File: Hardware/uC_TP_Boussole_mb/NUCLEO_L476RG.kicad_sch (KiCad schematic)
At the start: 1 part, among them U2 NUCLEO_L476RG

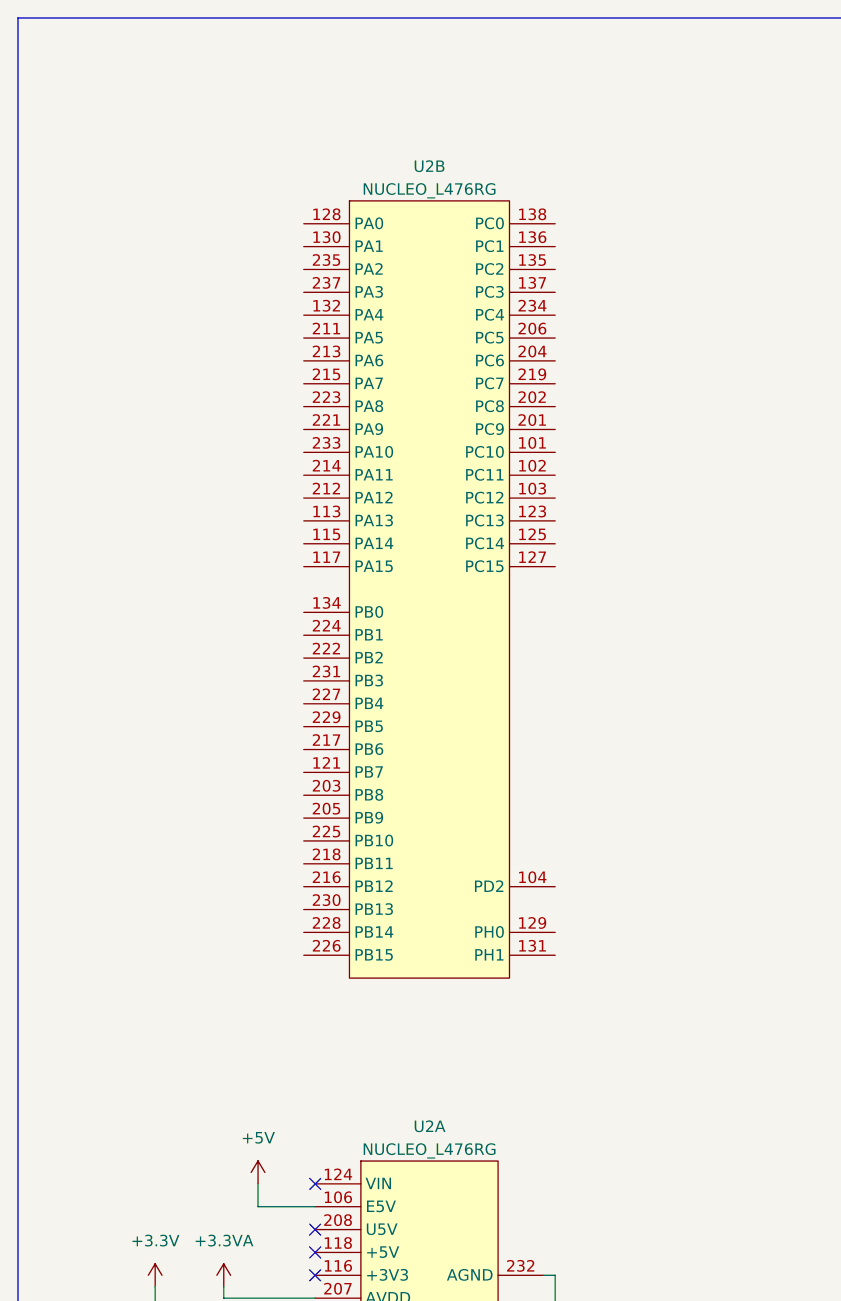
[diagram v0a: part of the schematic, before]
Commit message: starting pin out nucleo
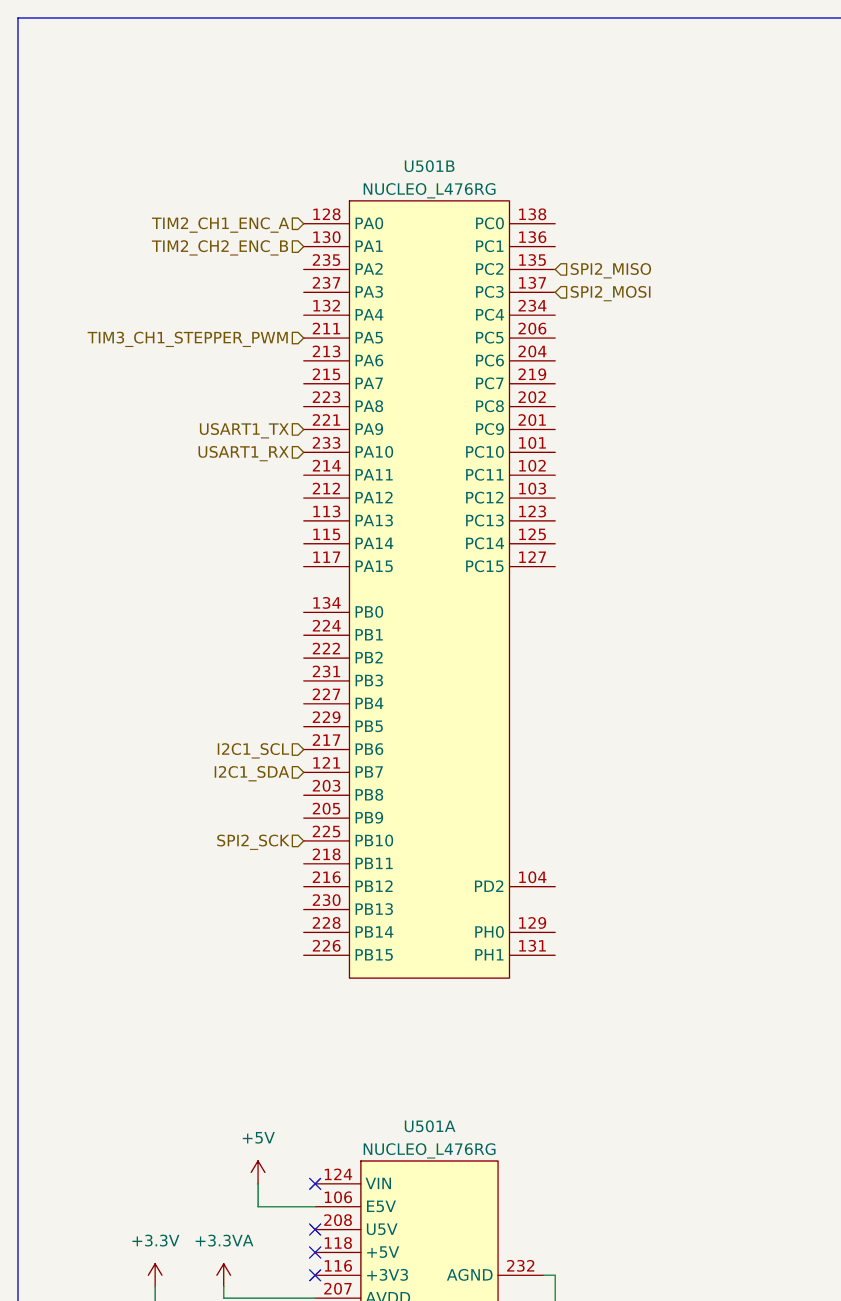
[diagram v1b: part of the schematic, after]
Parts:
- U501: renamed from U2; footprint WITNS:ST_NUCLEO_64 -> libs:ST_NUCLEO_64
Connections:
- net I2C1_SDA: now reaches U501.121 (PB7)
- net TIM2_CH1_ENC_A: now reaches U501.128 (PA0)
- net TIM2_CH2_ENC_B: now reaches U501.130 (PA1)
- net SPI2_MISO: now reaches U501.135 (PC2)
- net SPI2_MOSI: now reaches U501.137 (PC3)
- net TIM3_CH1_STEPPER_PWM: now reaches U501.211 (PA5)
- net I2C1_SCL: now reaches U501.217 (PB6)
- net USART1_TX: now reaches U501.221 (PA9)
- net SPI2_SCK: now reaches U501.225 (PB10)
- net USART1_RX: now reaches U501.233 (PA10)
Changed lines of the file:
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@@
+		)
+	)
+	(hierarchical_label "I2C1_SCL"
+		(shape input)
+		(at 46.99 95.25 180)
+		(fields_autoplaced yes)
+		(effects
+			(font
+				(size 1.27 1.27)
+			)
+			(justify right)
+		)
+	)
+	(hierarchical_label "TIM2_CH1_ENC_A"
+		(shape input)
+		(at 46.99 36.83 180)
+		(fields_autoplaced yes)
+		(effects
+			(font
+				(size 1.27 1.27)
+			)
+			(justify right)
+		)
+	)
+	(hierarchical_label "SPI2_MISO"
+		(shape input)
+		(at 74.93 41.91 0)
+		(fields_autoplaced yes)
+		(effects
+			(font
+				(size 1.27 1.27)
+			)
+			(justify left)
+		)
+	)
+	(hierarchical_label "SPI2_SCK"
+		(shape input)
+		(at 46.99 105.41 180)
+		(fields_autoplaced yes)
+		(effects
+			(font
+				(size 1.27 1.27)
+			)
+			(justify right)
+		)
+	)
+	(hierarchical_label "USART1_TX"
+		(shape input)
+		(at 46.99 59.69 180)
+		(fields_autoplaced yes)
+		(effects
+			(font
+				(size 1.27 1.27)
+			)
+			(justify right)
+		)
+	)
+	(hierarchical_label "TIM2_CH2_ENC_B"
+		(shape input)
+		(at 46.99 39.37 180)
+		(fields_autoplaced yes)
+		(effects
+			(font
+				(size 1.27 1.27)
+			)
+			(justify right)
+		)
+	)
+	(hierarchical_label "I2C1_SDA"
+		(shape input)
+		(at 46.99 97.79 180)
+		(fields_autoplaced yes)
+		(effects
+			(font
+				(size 1.27 1.27)
+			)
+			(justify right)
+		)
+	)
+	(hierarchical_label "SPI2_MOSI"
+		(shape input)
+		(at 74.93 44.45 0)
+		(fields_autoplaced yes)
+		(effects
+			(font
+				(size 1.27 1.27)
+			)
+			(justify left)
+		)
+	)
+	(hierarchical_label "USART1_RX"
+		(shape input)
+		(at 46.99 62.23 180)
+		(fields_autoplaced yes)
+		(effects
+			(font
+				(size 1.27 1.27)
+			)
+			(justify right)
+		)
+	)
+	(hierarchical_label "TIM3_CH1_STEPPER_PWM"
+		(shape input)
+		(at 46.99 49.53 180)
+		(fields_autoplaced yes)
+		(effects
+			(font
+				(size 1.27 1.27)
+			)
+			(justify right)
 		)
 	)
@@
 		(dnp no)
 		(fields_autoplaced yes)
-		(property "Reference" "U2"
+		(property "Reference" "U501"
 			(at 60.96 30.48 0)
 			(effects
@@
 			)
 		)
-		(property "Footprint" "WITNS:ST_NUCLEO_64"
+		(property "Footprint" "libs:ST_NUCLEO_64"
 			(at 60.96 54.61 0)
 			(effects
@@
 			(project "uC_TP_Boussole_mb"
 				(path "/2e9feef3-d2ce-488a-99fa-e1de5099ffc3/05c5487e-de82-4573-ad81-720c1b2881f4"
-					(reference "U2")
+					(reference "U501")
 					(unit 2)
 				)
@@
 		(dnp no)
 		(fields_autoplaced yes)
-		(property "Reference" "#PWR05"
+		(property "Reference" "#PWR0501"
 			(at 30.48 158.75 0)
 			(effects
@@
 			(project "uC_TP_Boussole_mb"
 				(path "/2e9feef3-d2ce-488a-99fa-e1de5099ffc3/05c5487e-de82-4573-ad81-720c1b2881f4"
-					(reference "#PWR05")
+					(reference "#PWR0501")
 					(unit 1)
 				)
@@
 		(dnp no)
 		(fields_autoplaced yes)
-		(property "Reference" "#PWR06"
+		(property "Reference" "#PWR0502"
 			(at 38.1 158.75 0)
 			(effects
@@
 			(project "uC_TP_Boussole_mb"
 				(path "/2e9feef3-d2ce-488a-99fa-e1de5099ffc3/05c5487e-de82-4573-ad81-720c1b2881f4"
-					(reference "#PWR06")
+					(reference "#PWR0502")
 					(unit 1)
 				)
@@
 		(dnp no)
 		(fields_autoplaced yes)
-		(property "Reference" "#PWR08"
+		(property "Reference" "#PWR0504"
 			(at 74.93 180.34 0)
 			(effects
@@
 			(project "uC_TP_Boussole_mb"
 				(path "/2e9feef3-d2ce-488a-99fa-e1de5099ffc3/05c5487e-de82-4573-ad81-720c1b2881f4"
-					(reference "#PWR08")
+					(reference "#PWR0504")
 					(unit 1)
 				)
@@
 		(dnp no)
 		(fields_autoplaced yes)
-		(property "Reference" "#PWR07"
+		(property "Reference" "#PWR0503"
 			(at 41.91 147.32 0)
 			(effects
@@
 			(project "uC_TP_Boussole_mb"
 				(path "/2e9feef3-d2ce-488a-99fa-e1de5099ffc3/05c5487e-de82-4573-ad81-720c1b2881f4"
-					(reference "#PWR07")
+					(reference "#PWR0503")
 					(unit 1)
 				)
@@
 		(dnp no)
 		(fields_autoplaced yes)
-		(property "Reference" "U2"
+		(property "Reference" "U501"
 			(at 60.96 137.16 0)
 			(effects
@@
 			)
 		)
-		(property "Footprint" "WITNS:ST_NUCLEO_64"
+		(property "Footprint" "libs:ST_NUCLEO_64"
 			(at 60.96 134.62 0)
 			(effects
@@
 			(project "uC_TP_Boussole_mb"
 				(path "/2e9feef3-d2ce-488a-99fa-e1de5099ffc3/05c5487e-de82-4573-ad81-720c1b2881f4"
-					(reference "U2")
+					(reference "U501")
 					(unit 1)
 				)

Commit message: update ppcb
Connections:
- net ENC_BTN: now reaches U501.117 (PA15)
- net V_Imes: now reaches U501.132 (PA4)
- net MAGNETO_INT: now reaches U501.134 (PB0)
- net MAGNETO_STATUS: now reaches U501.136 (PC1)
- net SPI_CS: now reaches U501.138 (PC0)
- net STEPPER_DIR: now reaches U501.213 (PA6)
- net STEPPER_MS1: now reaches U501.214 (PA11)
- net STEPPER_ENN: now reaches U501.215 (PA7)
- net STEPPER_MS2: now reaches U501.216 (PB12)
- net GPS_PPS: now reaches U501.234 (PC4)
- net GPS_EN: now reaches U501.235 (PA2)
- net +3.3V: no longer names the net of U501.105 (VDD)
- net +3.3VA: no longer names the net of U501.207 (AVDD)
- net +5V renamed E5V
- no-connect marks 8 -> 18

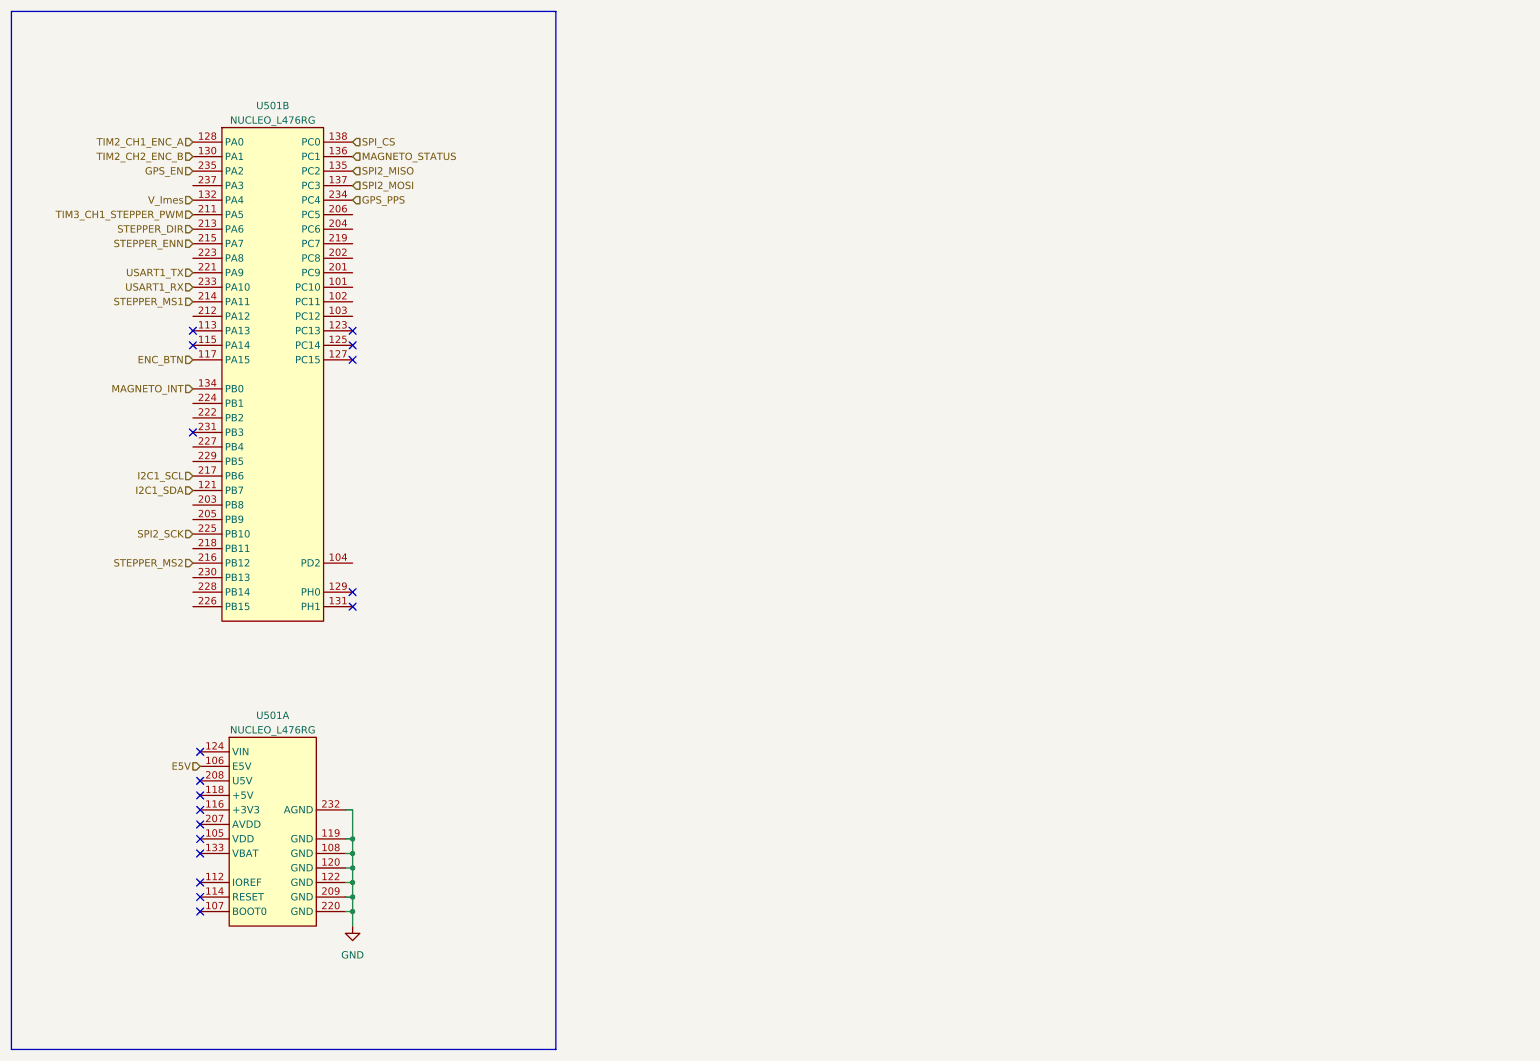
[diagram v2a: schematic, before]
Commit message: update schematic
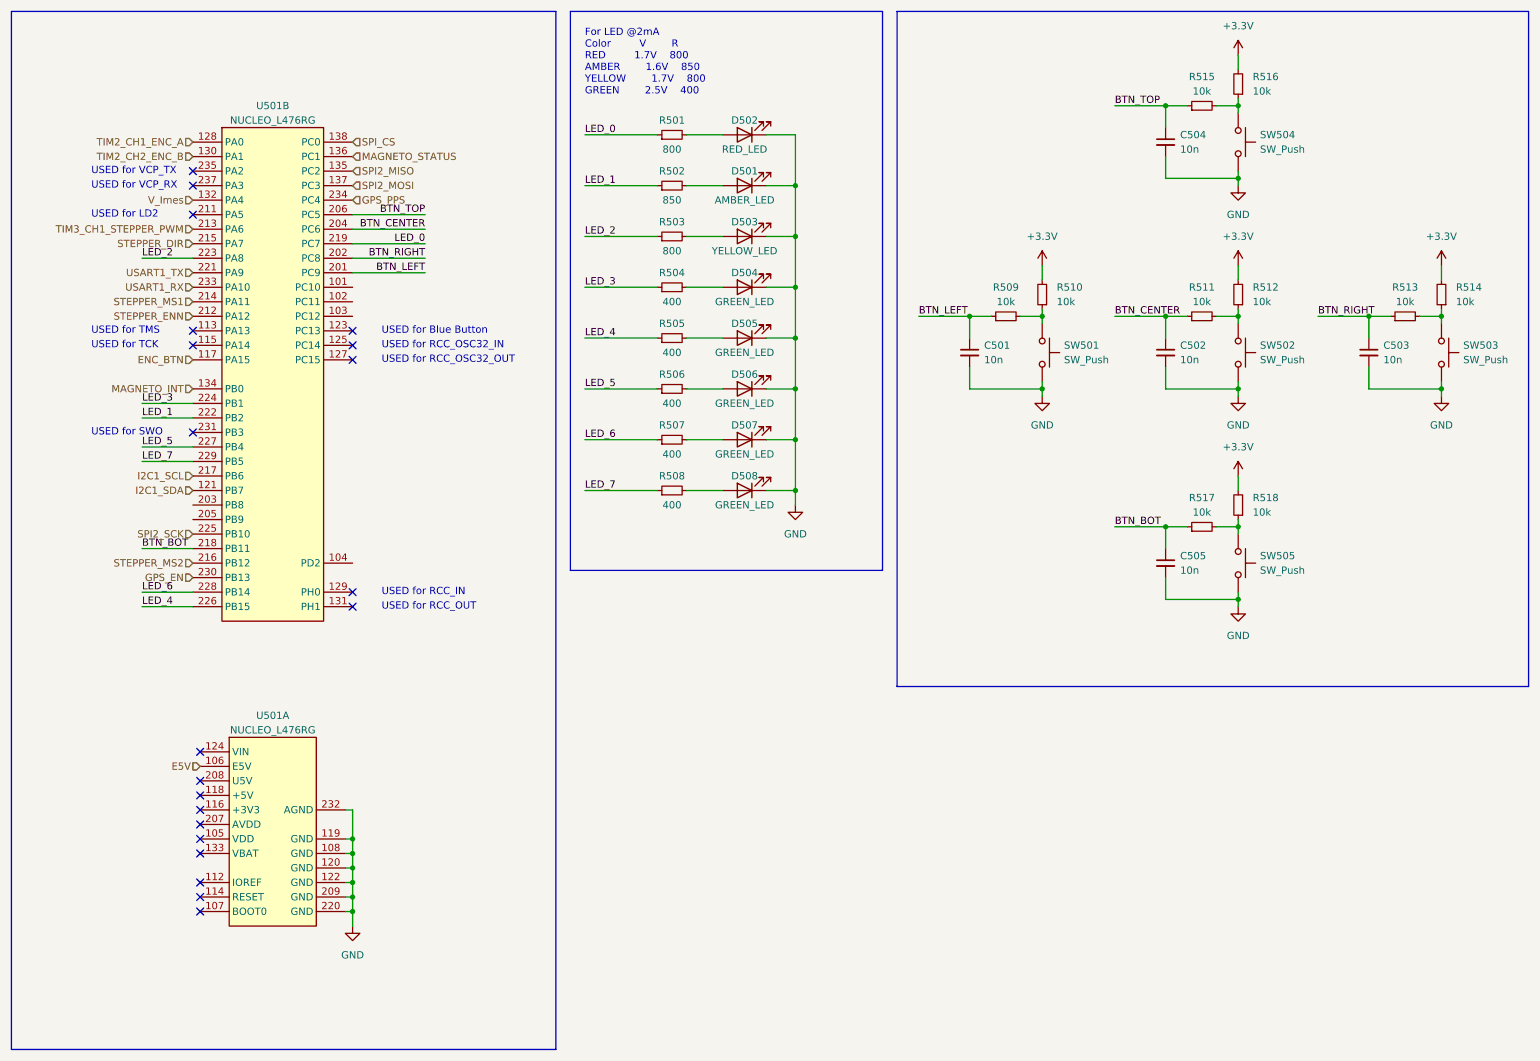
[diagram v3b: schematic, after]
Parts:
- added C501, C502, C503, C504, C505: 10n, Capacitor_SMD:C_0402_1005Metric, symbol Device:C_Small
- added D501: AMBER_LED, LED_SMD:LED_0603_1608Metric, symbol Device:LED
- added D502: RED_LED, LED_SMD:LED_0603_1608Metric, symbol Device:LED
- added D503: YELLOW_LED, LED_SMD:LED_0603_1608Metric, symbol Device:LED
- added D504, D505, D506, D507, D508: GREEN_LED, LED_SMD:LED_0603_1608Metric, symbol Device:LED
- added R501, R503: 800, Resistor_SMD:R_0402_1005Metric, symbol Device:R_Small
- added R502: 850, Resistor_SMD:R_0402_1005Metric, symbol Device:R_Small
- added R504, R505, R506, R507, R508: 400, Resistor_SMD:R_0402_1005Metric, symbol Device:R_Small
- added R509, R510, R511, R512, R513, R514, R515, R516, R517, R518: 10k, Resistor_SMD:R_0402_1005Metric, symbol Device:R_Small
- added SW501, SW502, SW503, SW504, SW505: SW_Push, Button_Switch_SMD:SW_Push_1P1T_NO_6x6mm_H9.5mm, symbol Switch:SW_Push
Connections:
- net GND: now also C501.2, C502.2, C503.2, C504.2, C505.2, D501.1 (K), D502.1 (K), D503.1 (K), D504.1 (K), D505.1 (K), D506.1 (K), D507.1 (K), D508.1 (K), SW501.2, SW502.2, SW503.2, SW504.2, SW505.2
- net GPS_EN: now also U501.230 (PB13); no longer U501.235 (PA2)
- net STEPPER_DIR: now also U501.215 (PA7); no longer U501.213 (PA6)
- net STEPPER_ENN: now also U501.212 (PA12); no longer U501.215 (PA7)
- net TIM3_CH1_STEPPER_PWM: now also U501.213 (PA6); no longer U501.211 (PA5)
- net BTN_LEFT: now reaches U501.201 (PC9)
- net BTN_LEFT: now also C501.1, R509.1
- net BTN_RIGHT: now reaches U501.202 (PC8)
- net BTN_RIGHT: now also C503.1, R513.1
- net BTN_CENTER: now reaches U501.204 (PC6)
- net BTN_CENTER: now also C502.1, R511.1
- net BTN_TOP: now reaches U501.206 (PC5)
- net BTN_TOP: now also C504.1, R515.1
- net BTN_BOT: now reaches U501.218 (PB11)
- net BTN_BOT: now also C505.1, R517.1
- net LED_0: now reaches U501.219 (PC7)
- net LED_0: now also R501.1
- net LED_1: now reaches U501.222 (PB2)
- net LED_1: now also R502.1
- net LED_2: now reaches U501.223 (PA8)
- net LED_2: now also R503.1
- net LED_3: now reaches U501.224 (PB1)
- net LED_3: now also R504.1
- net LED_4: now reaches U501.226 (PB15)
- net LED_4: now also R505.1
- net LED_5: now reaches U501.227 (PB4)
- net LED_5: now also R506.1
- net LED_6: now reaches U501.228 (PB14)
- net LED_6: now also R507.1
- net LED_7: now reaches U501.229 (PB5)
- net LED_7: now also R508.1
- new net: D504.2 (A), R504.2
- new net: D507.2 (A), R507.2
- new net: R513.2, R514.1, SW503.1
- new net: D503.2 (A), R503.2
- new net: D502.2 (A), R501.2
- new net: R511.2, R512.1, SW502.1
- new net: D505.2 (A), R505.2
- new net: R509.2, R510.1, SW501.1
- new net: D508.2 (A), R508.2
- new net: R515.2, R516.1, SW504.1
- new net: D506.2 (A), R506.2
- new net: D501.2 (A), R502.2
- new net: R517.2, R518.1, SW505.1
- new net +3.3V: R510.2, R512.2, R514.2, R516.2, R518.2
- no-connect marks 18 -> 21
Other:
- note added: "For LED @2mA Color V R RED 1.7V 800 AMBER 1.6V 850 YELLOW 1.7V 800 GREEN 2.5V 400"
- note added: "USED for Blue Button"
- note added: "USED for LD2"
- note added: "USED for RCC_IN"
- note added: "USED for RCC_OSC32_IN"
- note added: "USED for RCC_OSC32_OUT"
- note added: "USED for RCC_OUT"
- note added: "USED for SWO"
- note added: "USED for TCK"
- note added: "USED for TMS"
- note added: "USED for VCP_RX"
- note added: "USED for VCP_TX"

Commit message: ddd
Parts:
- added J501, J502, J503: Conn_01x06, Connector_PinHeader_2.54mm:PinHeader_1x06_P2.54mm_Vertical, symbol Connector_Generic:Conn_01x06
- renumbered C504 to C502, C502 to C503, C505 to C504, C503 to C505, D502 to D501, D501 to D502, R515 to R511, R511 to R512, R517 to R513, R516 to R514, R512 to R515, R518 to R516, R513 to R517, R514 to R518, SW504 to SW502, SW502 to SW503, SW505 to SW504, SW503 to SW505
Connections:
- net +3.3V: now also J503.1 (Pin_1), J503.2 (Pin_2), J503.3 (Pin_3), J503.4 (Pin_4), J503.5 (Pin_5), J503.6 (Pin_6)
- net GND: now also J502.1 (Pin_1), J502.2 (Pin_2), J502.3 (Pin_3), J502.4 (Pin_4), J502.5 (Pin_5), J502.6 (Pin_6)
- net PC10: now reaches U501.101 (PC10)
- net PC10: now also J501.1 (Pin_1)
- net PC11: now reaches U501.102 (PC11)
- net PC11: now also J501.2 (Pin_2)
- net PC12: now reaches U501.103 (PC12)
- net PC12: now also J501.3 (Pin_3)
- net PD2: now reaches U501.104 (PD2)
- net PD2: now also J501.6 (Pin_6)
- net PB8: now reaches U501.203 (PB8)
- net PB8: now also J501.4 (Pin_4)
- net PB9: now reaches U501.205 (PB9)
- net PB9: now also J501.5 (Pin_5)
